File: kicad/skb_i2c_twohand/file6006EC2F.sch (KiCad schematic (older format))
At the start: 72 parts, among them SW1 SW_PUSH, SW10 SW_PUSH, SW11 SW_PUSH, SW12 SW_PUSH, SW13 SW_PUSH, SW14 SW_PUSH, SW17 SW_PUSH, SW18 SW_PUSH, SW19 SW_PUSH, SW2 SW_PUSH, SW20 SW_PUSH, SW21 SW_PUSH, SW22 SW_PUSH, SW25 SW_PUSH, SW26 SW_PUSH, SW27 SW_PUSH, SW28 SW_PUSH, SW29 SW_PUSH, SW3 SW_PUSH, SW30 SW_PUSH, SW33 SW_PUSH, SW34 SW_PUSH, SW35 SW_PUSH, SW36 SW_PUSH, SW37 SW_PUSH, SW38 SW_PUSH, SW4 SW_PUSH, SW41 SW_PUSH, SW42 SW_PUSH, SW43 SW_PUSH, SW44 SW_PUSH, SW45 SW_PUSH, SW46 SW_PUSH, SW5 SW_PUSH, SW6 SW_PUSH, SW9 SW_PUSH

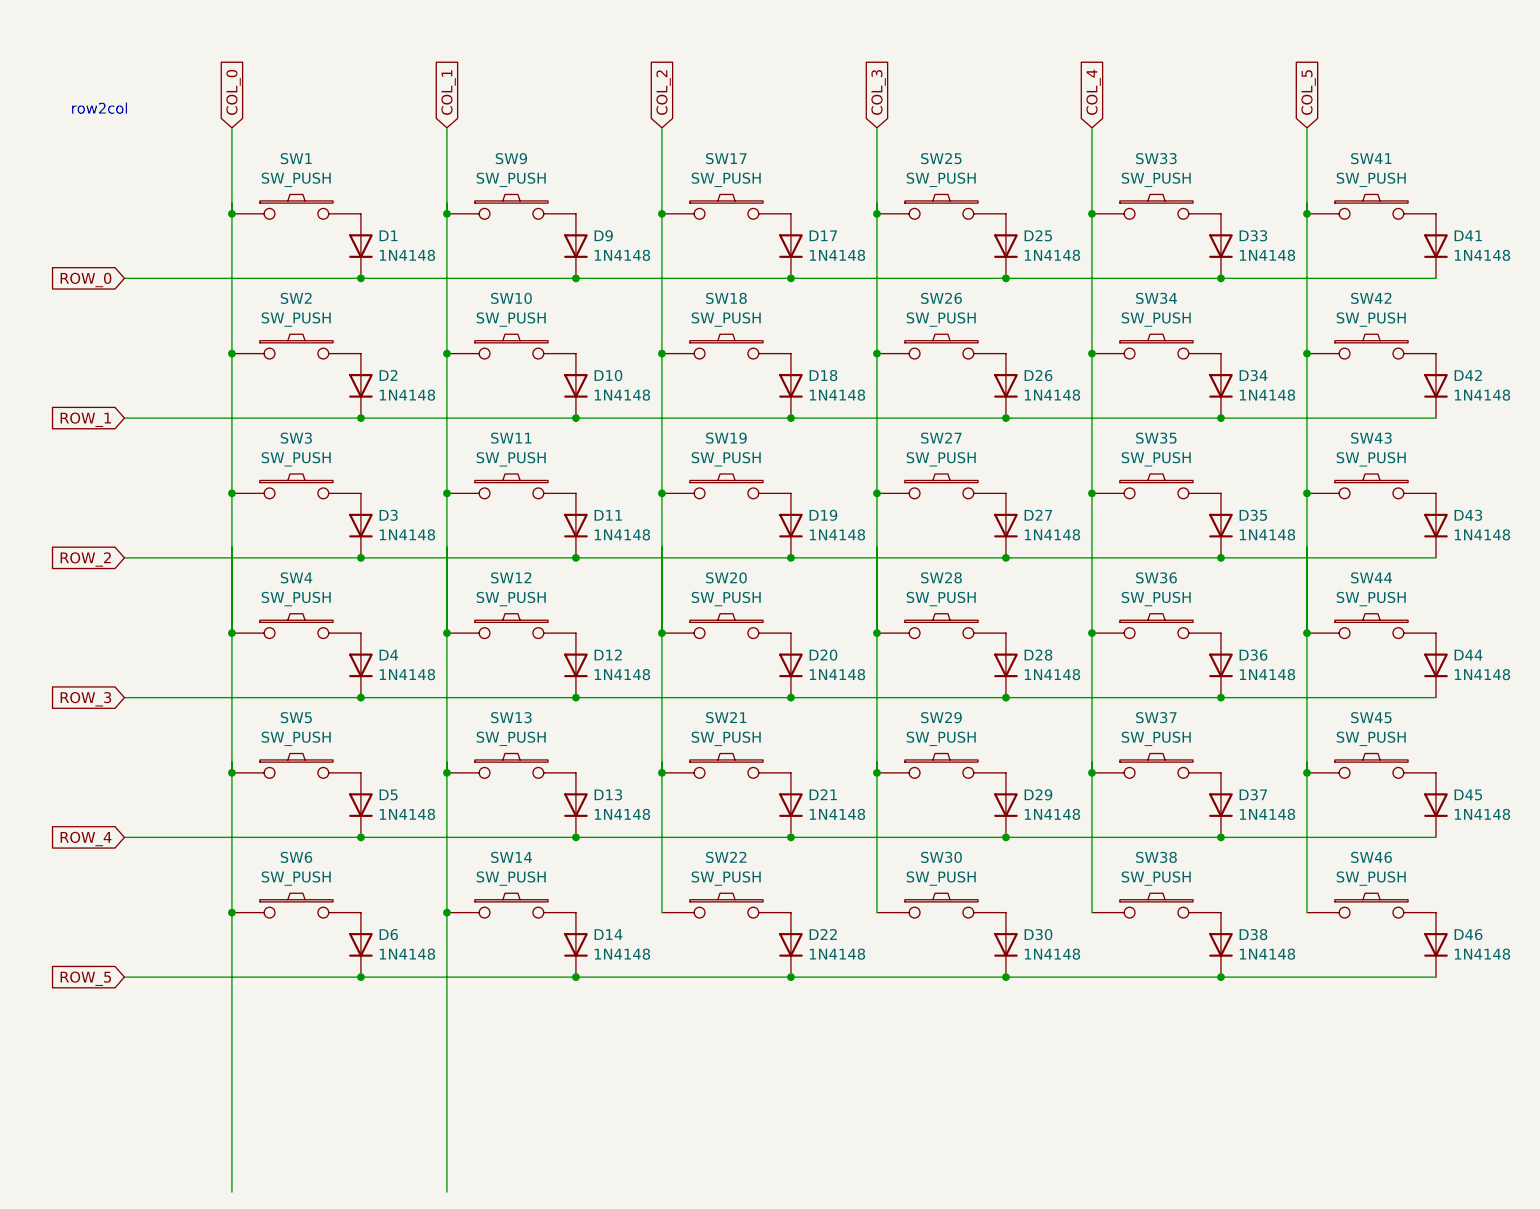
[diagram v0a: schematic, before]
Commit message: merge two keyboard schema in one project.
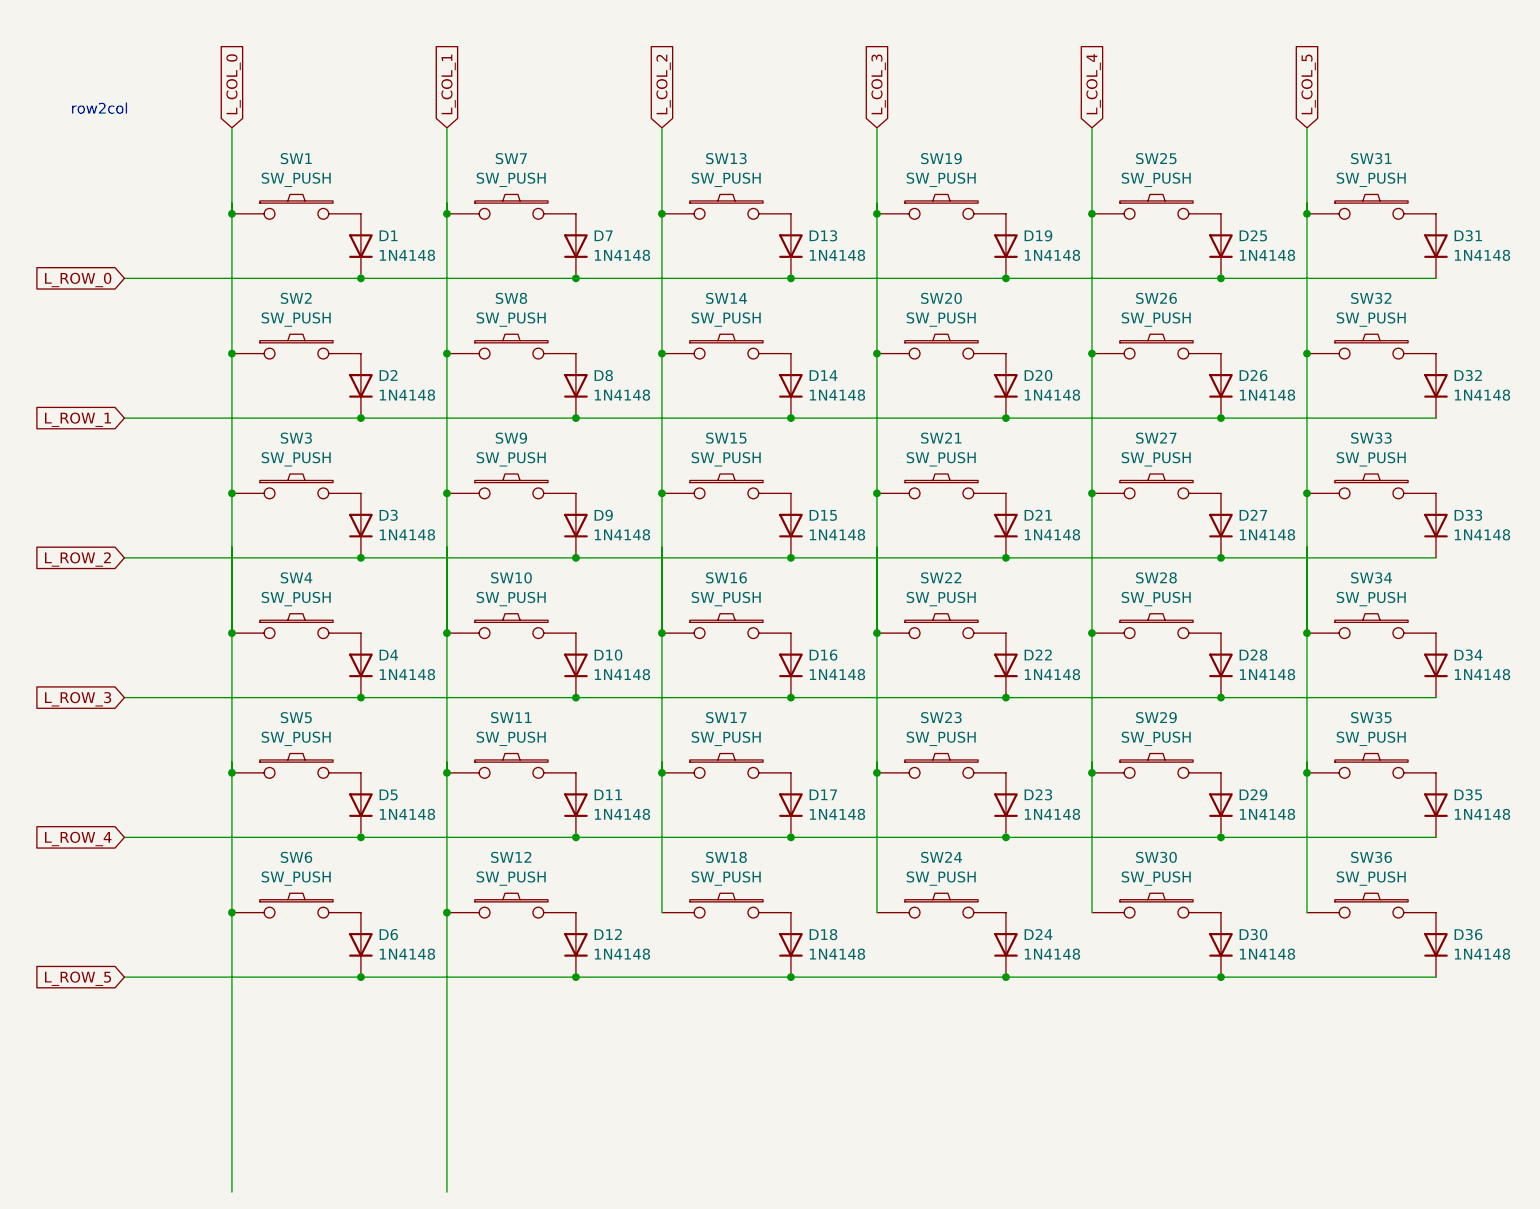
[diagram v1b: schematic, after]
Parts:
- renumbered D12 to D10, D13 to D11, D14 to D12, D17 to D13, D18 to D14, D19 to D15, D20 to D16, D21 to D17, D22 to D18, D25 to D19, D26 to D20, D27 to D21, D28 to D22, D29 to D23, D30 to D24, D33 to D25, D34 to D26, D35 to D27, D36 to D28, D37 to D29, D38 to D30, D41 to D31, D42 to D32, D43 to D33, D44 to D34, D45 to D35, D46 to D36, D9 to D7, D10 to D8, D11 to D9, SW12 to SW10, SW13 to SW11, SW14 to SW12, SW17 to SW13, SW18 to SW14, SW19 to SW15, SW20 to SW16, SW21 to SW17, SW22 to SW18, SW25 to SW19, SW26 to SW20, SW27 to SW21, SW28 to SW22, SW29 to SW23, SW30 to SW24, SW33 to SW25, SW34 to SW26, SW35 to SW27, SW36 to SW28, SW37 to SW29, SW38 to SW30, SW41 to SW31, SW42 to SW32, SW43 to SW33, SW44 to SW34, SW45 to SW35, SW46 to SW36, SW9 to SW7, SW10 to SW8, SW11 to SW9
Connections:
- net labels added: L_COL_0, L_COL_1, L_COL_2, L_COL_3, L_COL_4, L_COL_5, L_ROW_0, L_ROW_1, L_ROW_2, L_ROW_3, L_ROW_4, L_ROW_5
- net labels removed: COL_0, COL_1, COL_2, COL_3, COL_4, COL_5, ROW_0, ROW_1, ROW_2, ROW_3, ROW_4, ROW_5

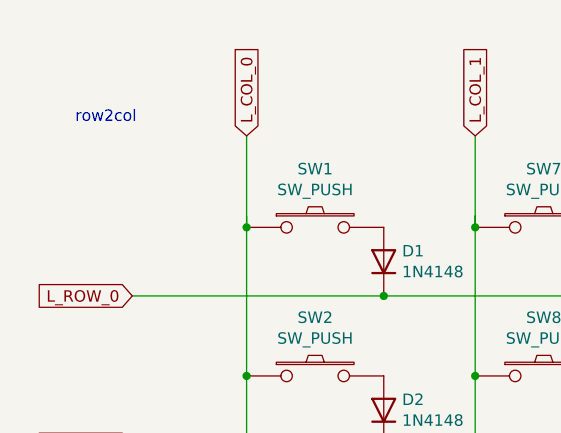
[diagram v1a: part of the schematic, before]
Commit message: modify row2col to col2row
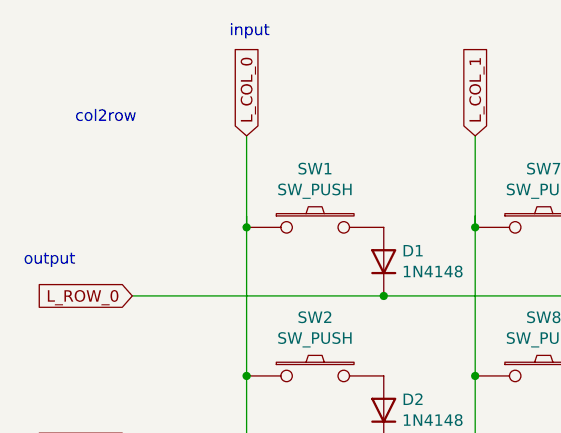
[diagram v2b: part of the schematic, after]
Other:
- note added: "col2row"
- note added: "input"
- note added: "output"
- note removed: "row2col"
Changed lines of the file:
@@
 Connection ~ 3600 2100
 Text Notes 850  1000 0    50   ~ 0
-row2col
+col2row
 $Comp
 L kbd:SW_PUSH SW?
@@
 Wire Wire Line
 	2600 4700 2600 6000
+Text Notes 1525 625  0    50   ~ 0
+input
+Text Notes 625  1625 0    50   ~ 0
+output
 $EndSCHEMATC
